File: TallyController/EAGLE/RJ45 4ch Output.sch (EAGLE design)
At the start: 10 parts, among them J1 RJHSE-5381-04

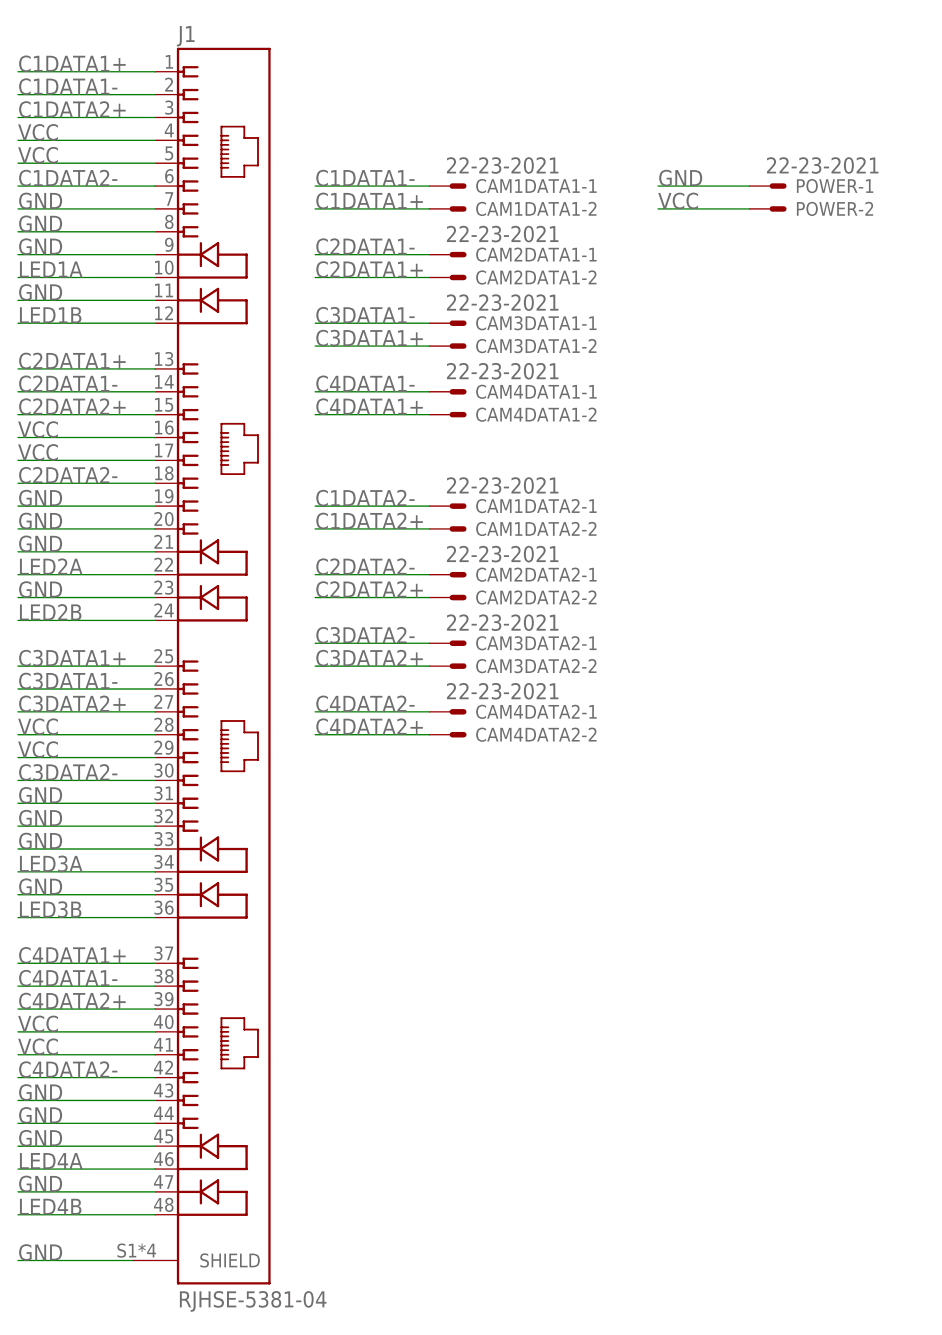
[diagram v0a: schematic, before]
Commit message: Go through and fix notation on RS485 wiring everywhere to use the standard A/B notation.
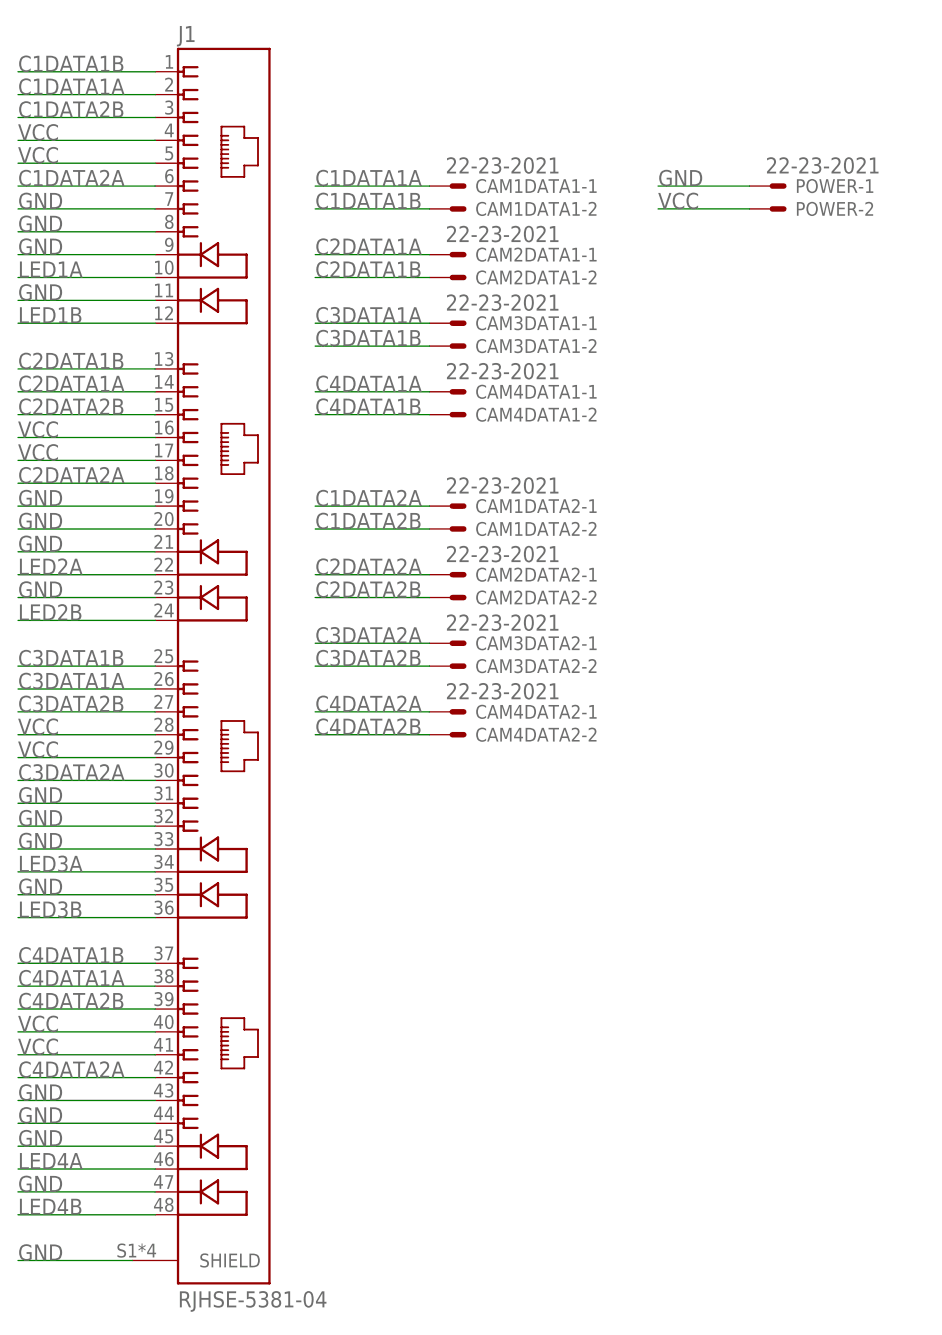
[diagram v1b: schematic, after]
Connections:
- net C1DATA1+ renamed C1DATA1B
- net C1DATA1- renamed C1DATA1A
- net C1DATA2+ renamed C1DATA2B
- net C1DATA2- renamed C1DATA2A
- net C2DATA1+ renamed C2DATA1B
- net C2DATA1- renamed C2DATA1A
- net C2DATA2+ renamed C2DATA2B
- net C2DATA2- renamed C2DATA2A
- net C3DATA1+ renamed C3DATA1B
- net C3DATA1- renamed C3DATA1A
- net C3DATA2+ renamed C3DATA2B
- net C3DATA2- renamed C3DATA2A
- net C4DATA1+ renamed C4DATA1B
- net C4DATA1- renamed C4DATA1A
- net C4DATA2+ renamed C4DATA2B
- net C4DATA2- renamed C4DATA2A
